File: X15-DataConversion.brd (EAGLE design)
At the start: 24.3 x 25.4 mm, 22 parts

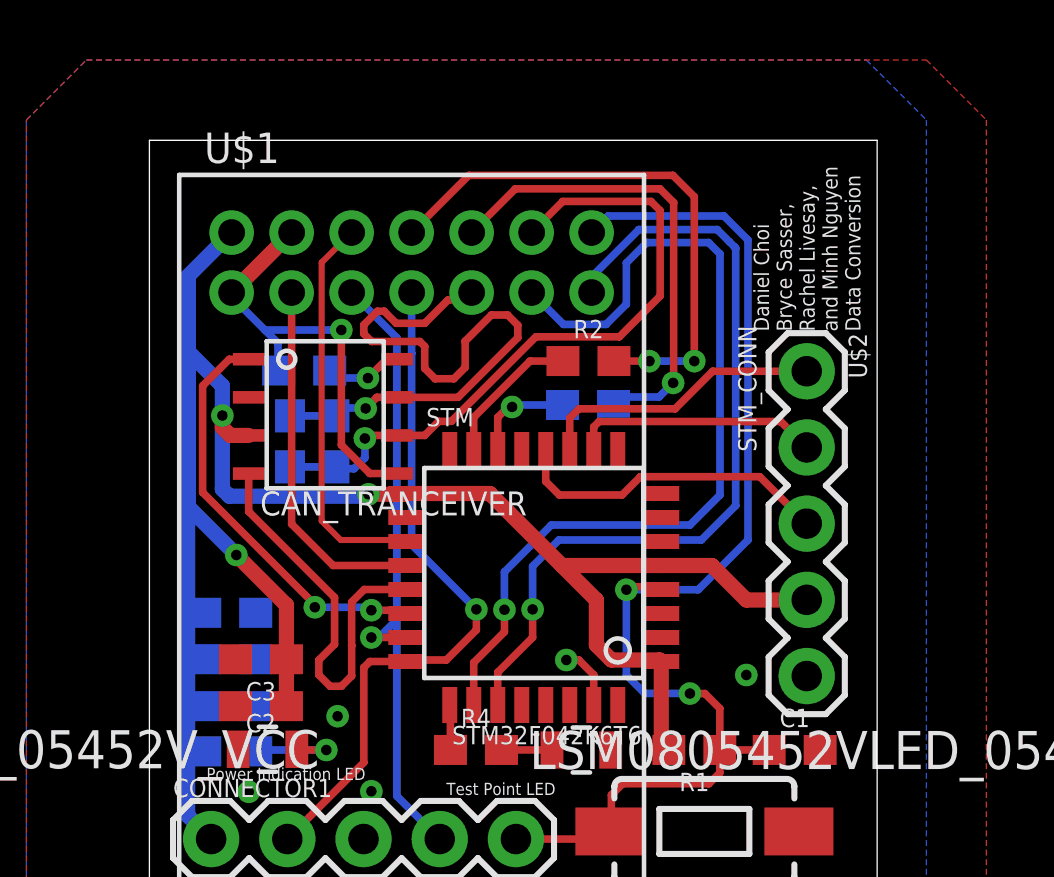
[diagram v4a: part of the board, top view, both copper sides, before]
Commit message: fixed some trace lengths and widths and angles
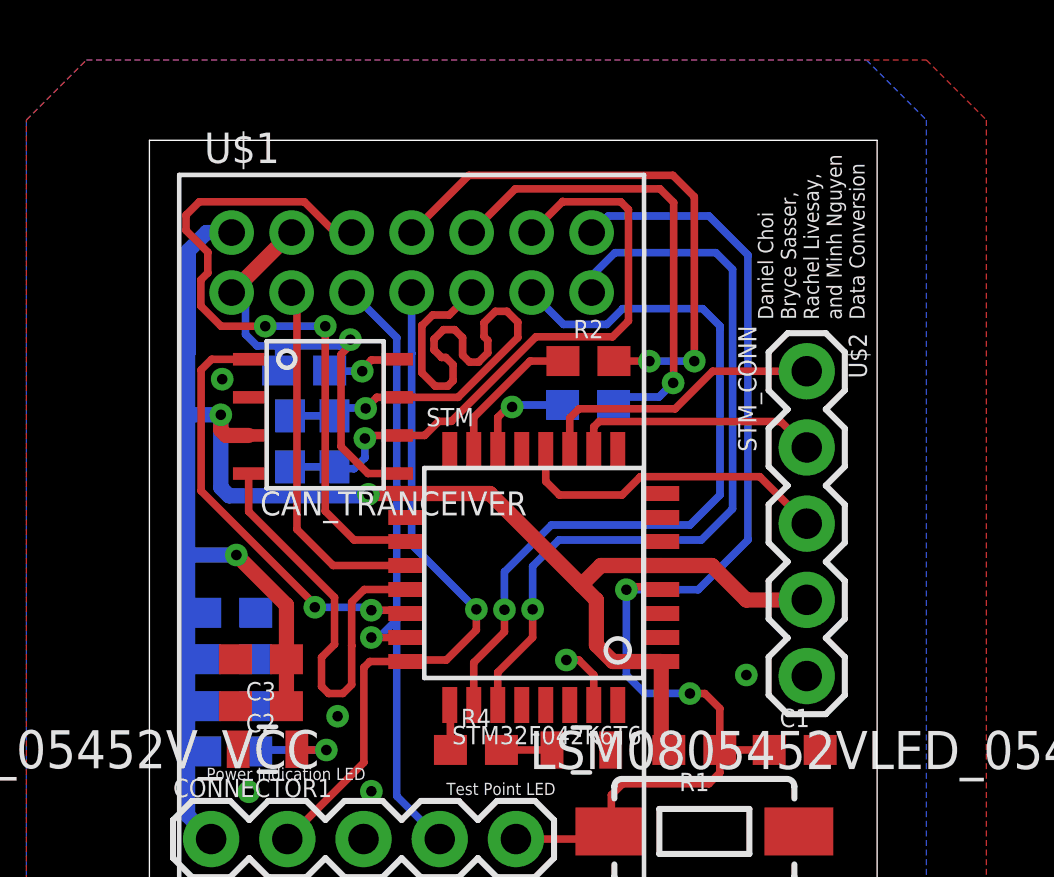
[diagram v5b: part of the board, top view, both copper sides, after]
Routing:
- net CLK: track 13.1 -> 23.3 mm, vias 0 -> 2
- net ALERT2: track 30.0 -> 25.9 mm
- net 3V3: track 67.8 -> 66.0 mm
- net CAN_L: track 22.9 -> 21.3 mm
- net ALERT1: track 27.5 -> 26.3 mm
- net GND: track 16.8 -> 17.1 mm, vias 6 -> 7

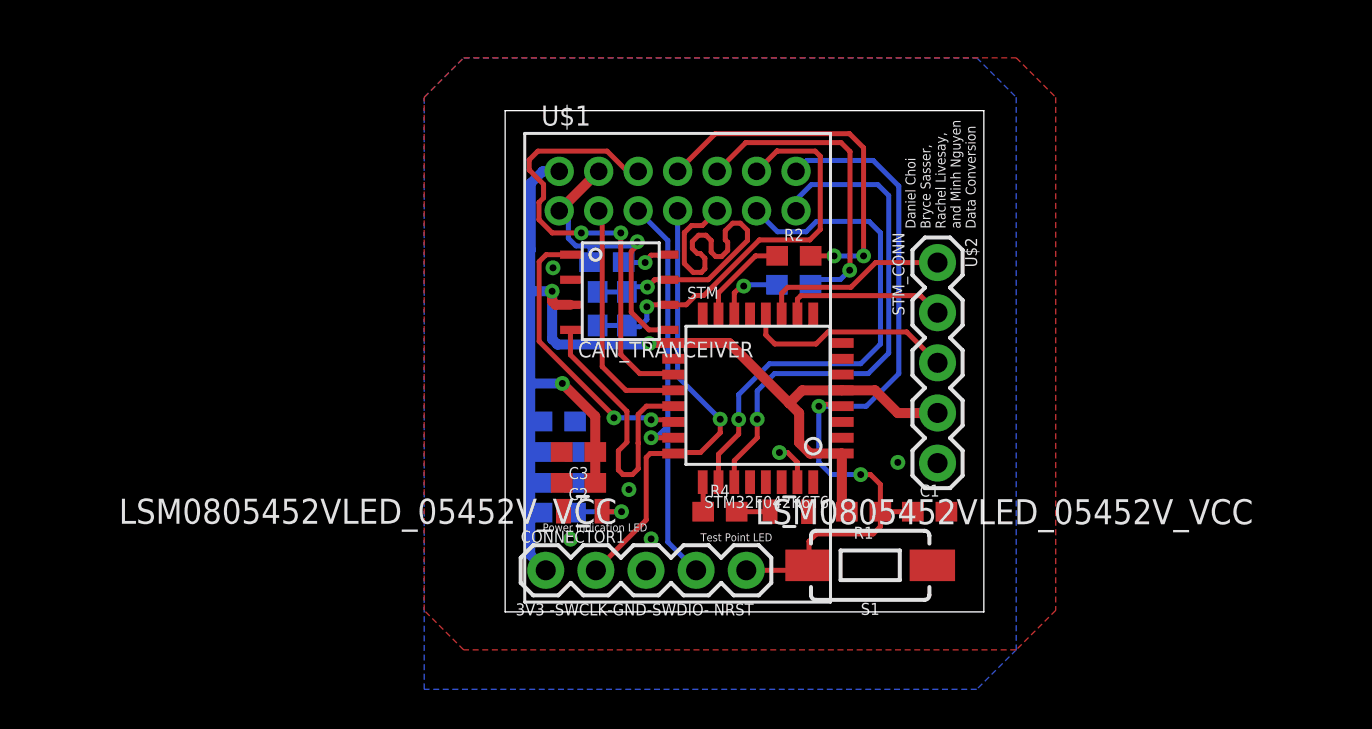
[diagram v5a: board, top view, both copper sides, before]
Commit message: used the wrong connector so fixed that
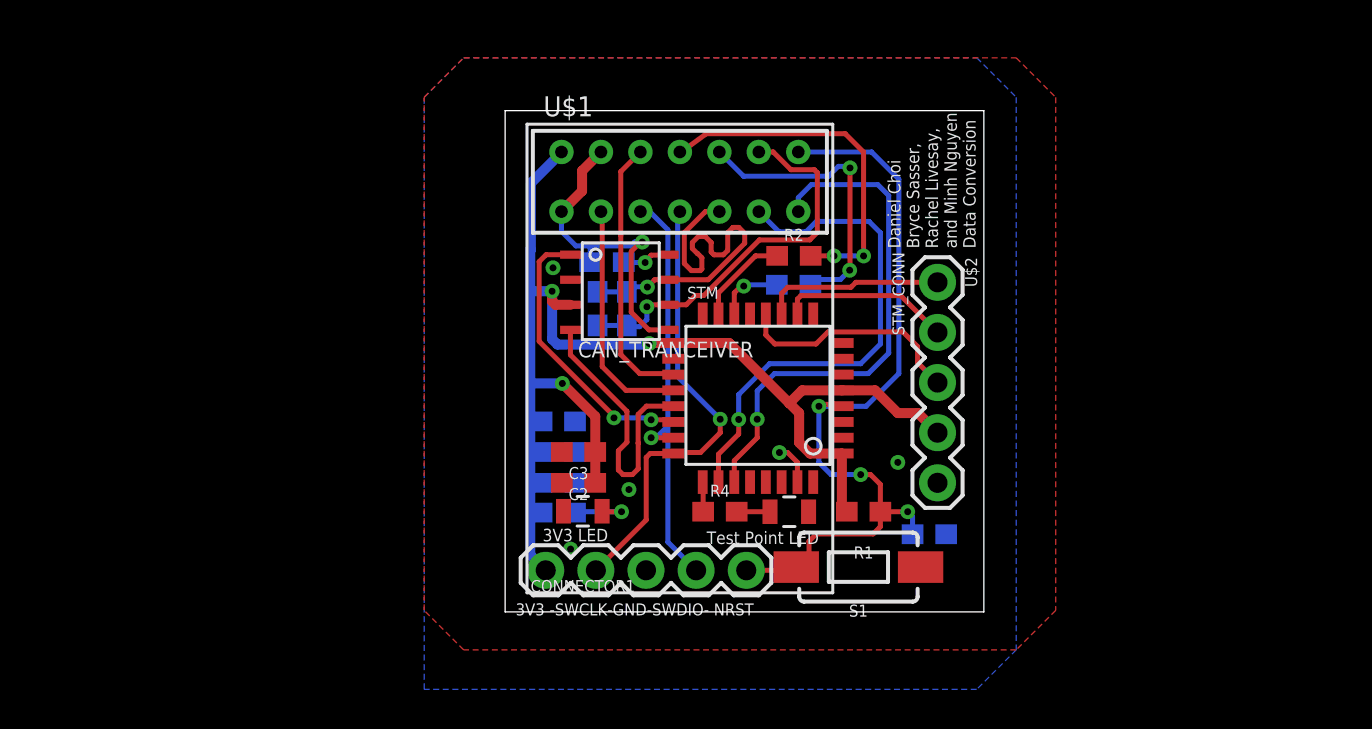
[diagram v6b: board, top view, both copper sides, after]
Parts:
- U$1: value DATACONV->BACKPLANE -> BACKPLANE->DATACONV; device X15-Data-Conversion-Parts:SAMTEC-CLT-107-01-X-D-DATACONV -> X15-Data-Conversion-Parts:SAMTEC-CLT-107-01-X-D-BACKPLANE
- moved C1 1.14 mm to (21.6, 3.86), flipped to the bottom, turned to 180 degrees
- moved U$2 1.00 mm to (22.0, 16.6)
- moved S1 0.60 mm to (18.0, 2.20)
- moved U$1 0.48 mm to (8.96, 21.7)
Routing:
- net CLK: track 23.3 -> 13.8 mm, vias 2 -> 0
- net GND: track 17.1 -> 18.4 mm, vias 7 -> 6
- net CAN_L: track 21.3 -> 20.1 mm
- net CAN_H: track 21.3 -> 20.1 mm
- net C2_1: track 15.8 -> 14.9 mm, vias 1 -> 2
- net 3V3: track 66.0 -> 66.9 mm
- net ADC_IN2: track 10.8 -> 11.7 mm
- net NRST: track 40.1 -> 40.8 mm, vias 2 -> 3
- net C2_2: track 18.7 -> 17.9 mm
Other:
- board text added: "3V3 LED"
- board text removed: "Power Indication LED"
